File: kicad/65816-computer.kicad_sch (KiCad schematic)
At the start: 0 parts

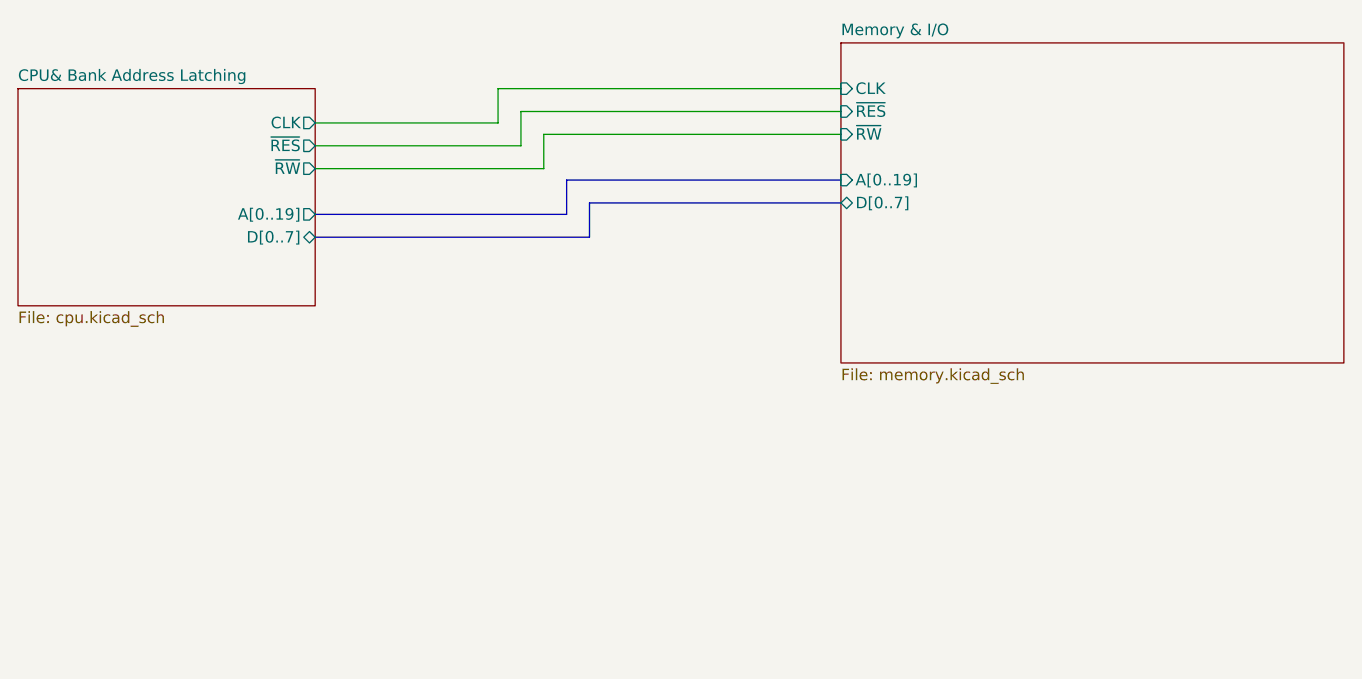
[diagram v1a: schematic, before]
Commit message: connect IRQ output of 65C22 to CPU NMI
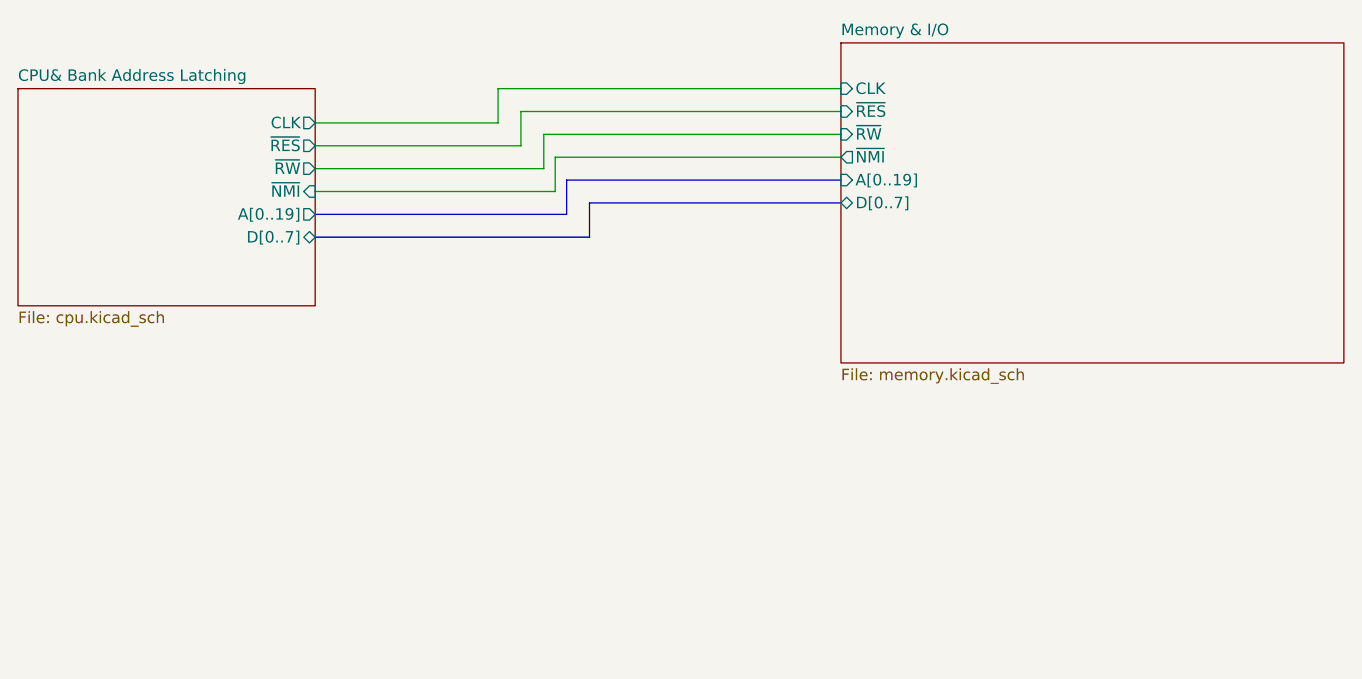
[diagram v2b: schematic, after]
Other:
- sheet CPU& Bank Address Latching ports: added ~{NMI}; removed none
- sheet Memory & I/O ports: added ~{NMI}; removed none
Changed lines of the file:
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@@
+    (stroke (width 0) (type default) (color 0 0 0 0))
+  )
+  (wire (pts (xy 142.24 93.98) (xy 142.24 97.79))
     (stroke (width 0) (type default) (color 0 0 0 0))
   )
@@
     (stroke (width 0) (type default) (color 0 0 0 0))
   )
+  (wire (pts (xy 142.24 97.79) (xy 115.57 97.79))
+    (stroke (width 0) (type default) (color 0 0 0 0))
+  )
   (bus (pts (xy 115.57 100.33) (xy 143.51 100.33))
     (stroke (width 0) (type default) (color 0 0 0 0))
@@
   )
   (bus (pts (xy 146.05 102.87) (xy 146.05 99.06))
+    (stroke (width 0) (type default) (color 0 0 0 0))
+  )
+  (wire (pts (xy 173.99 93.98) (xy 142.24 93.98))
     (stroke (width 0) (type default) (color 0 0 0 0))
   )
@@
       (effects (font (size 1.27 1.27)) (justify right))
     )
+    (pin "~{NMI}" input (at 115.57 97.79 0)
+      (effects (font (size 1.27 1.27)) (justify right))
+    )
   )
   (sheet (at 173.99 81.28) (size 55.88 35.56) (fields_autoplaced)
@@
       (effects (font (size 1.27 1.27)) (justify left))
     )
+    (pin "~{NMI}" output (at 173.99 93.98 180)
+      (effects (font (size 1.27 1.27)) (justify left))
+    )

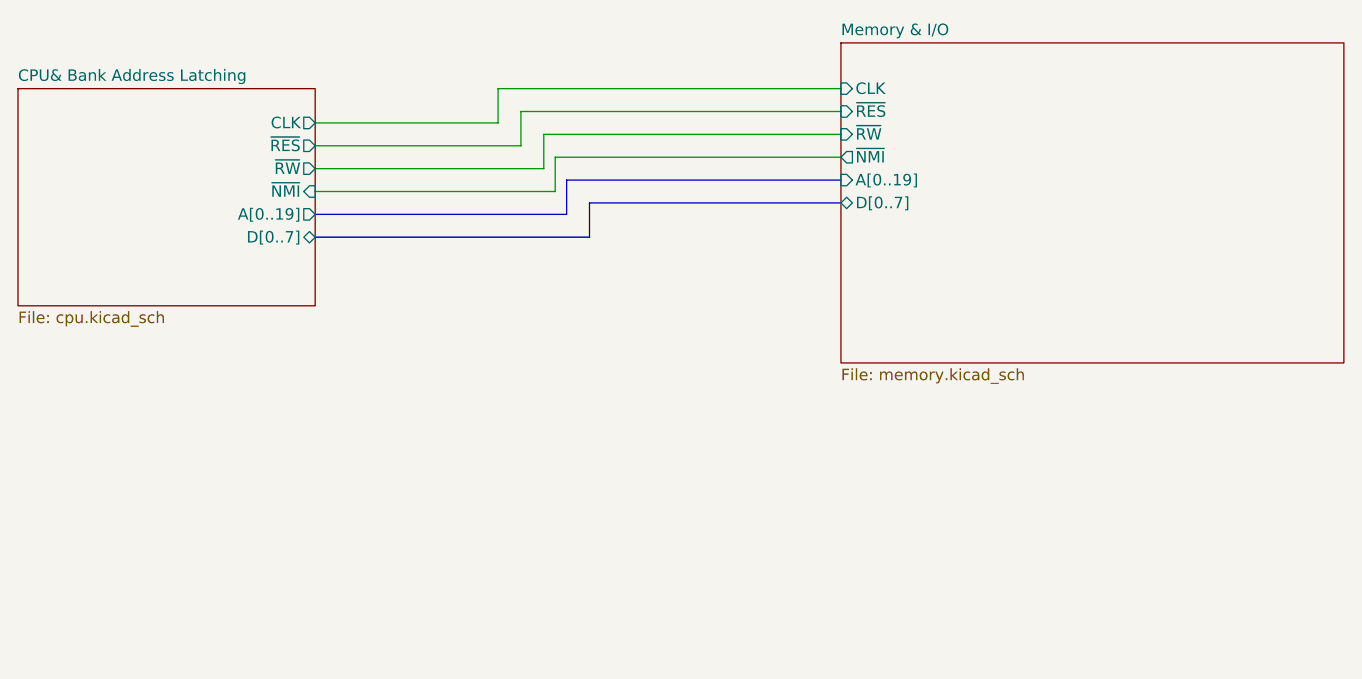
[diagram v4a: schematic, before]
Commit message: separate I/O schematic page, add SC16C752 for future use
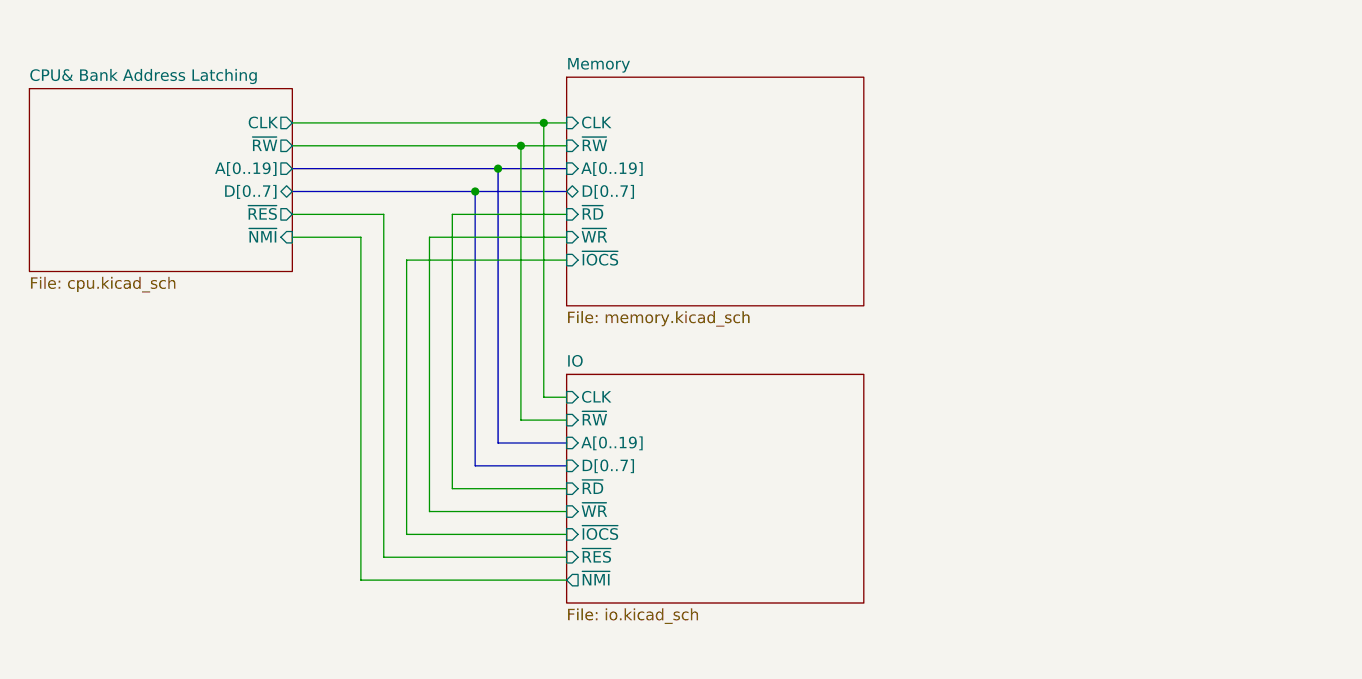
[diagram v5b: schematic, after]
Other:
- sheet Memory & I/O renamed Memory
- added sheet IO (io.kicad_sch)
- sheet Memory ports: added ~{IOCS}, ~{RD}, ~{WR}; removed ~{NMI}, ~{RES}

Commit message: connect UART to circuit
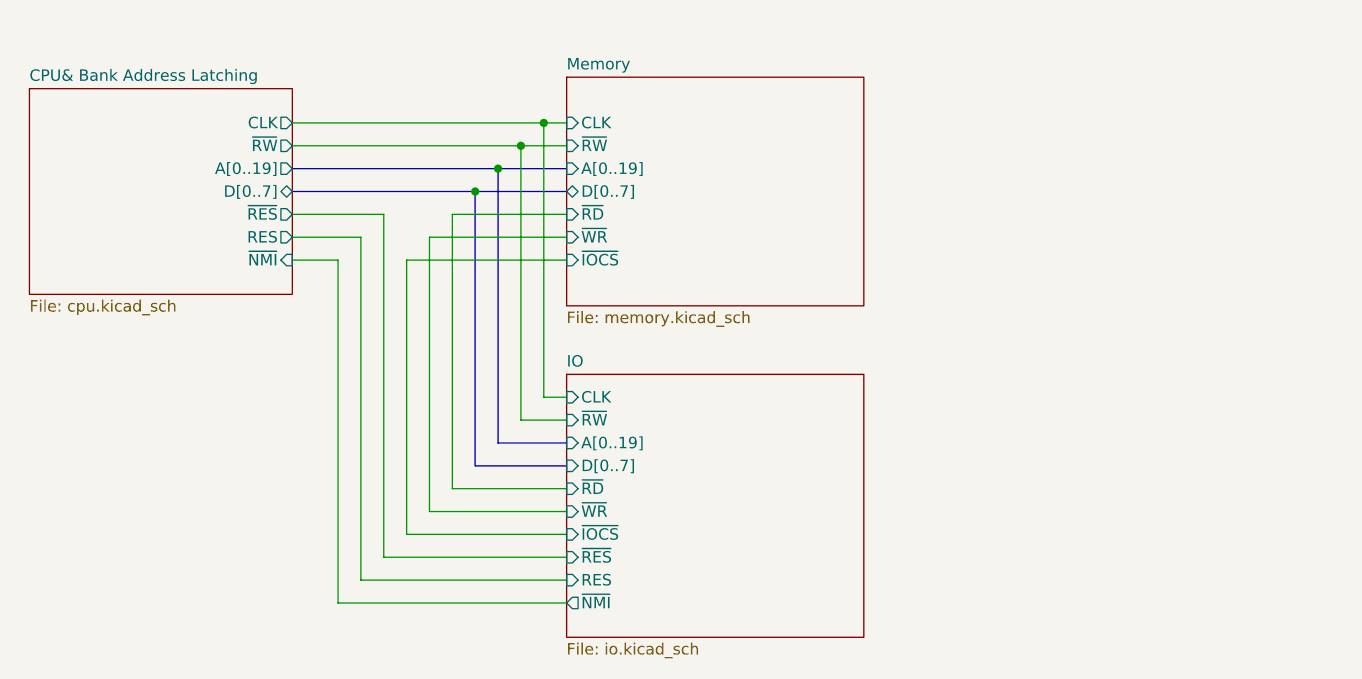
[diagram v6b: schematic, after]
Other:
- sheet CPU& Bank Address Latching ports: added RES; removed none
- sheet IO ports: added RES; removed none
